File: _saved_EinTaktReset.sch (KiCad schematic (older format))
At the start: 58 parts, among them IC1 74LS624, J1 3PinTerminalBlocktg, J2 3PinTerminalBlocktg, J3 2PinTerminalBlocktg, J4 3PinTerminalBlocktg, J5 2PinTerminalBlocktg, P1 CONN_02X10, P4 CONN_02X10, SW1 SPST, SW10 SPST, SW11 SPST, SW12 SPST, SW13 SPST, SW2 SWITCH_INV, SW3 SPST, SW4 SPST, SW5 SPST, SW6 SWITCH_INV, SW7 SPST, SW8 SPST, SW9 SPST, U1 74LS132, U2 74540En, U3 74HCT541_PWR, U4 74LS32, U5 74LS00

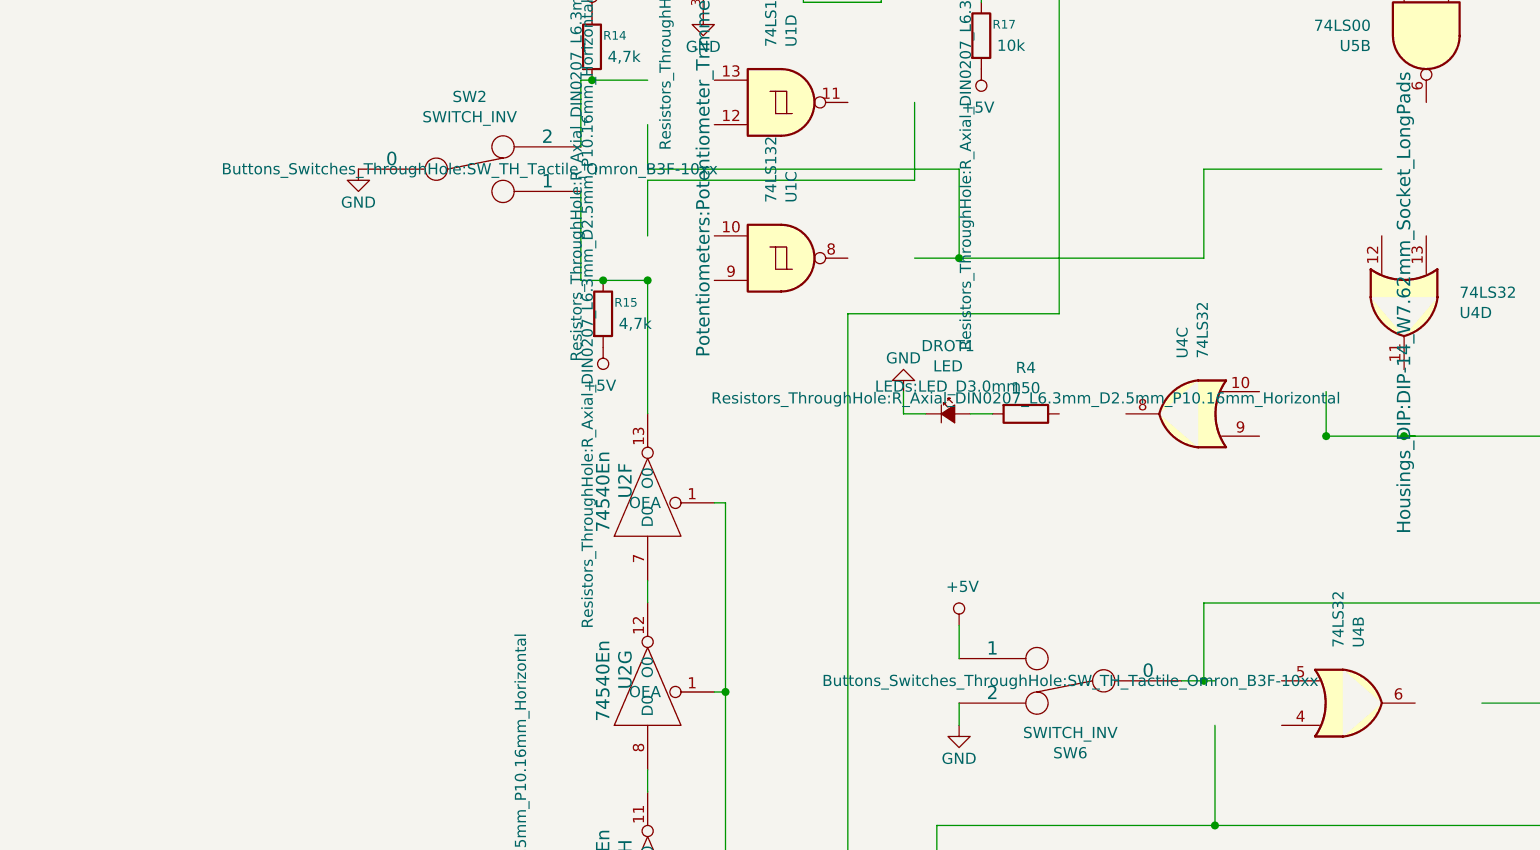
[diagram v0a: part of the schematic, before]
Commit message: Library für switches geadded
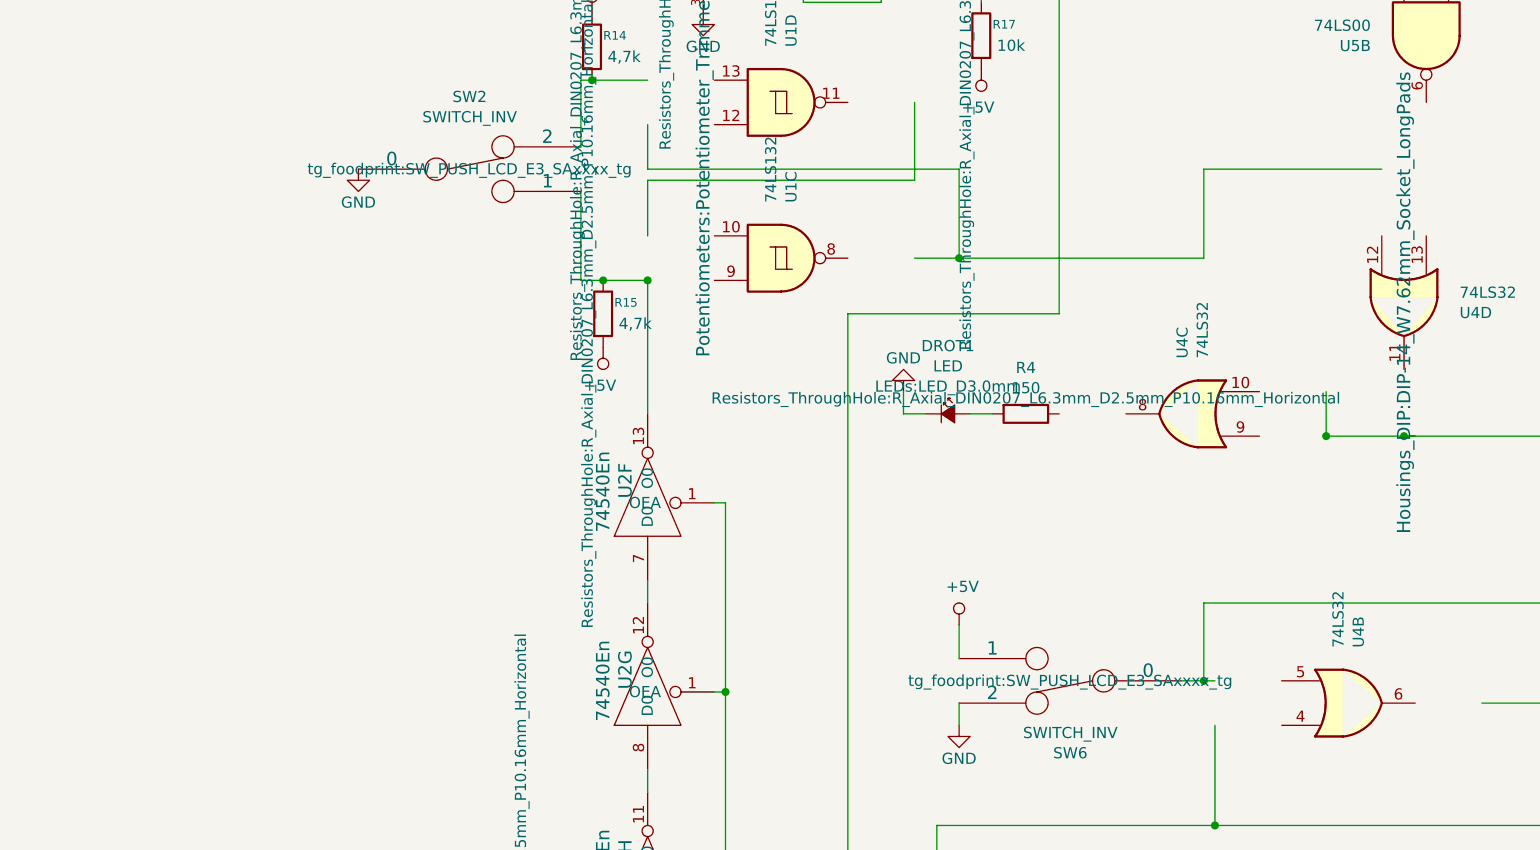
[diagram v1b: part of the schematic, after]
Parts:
- SW2, SW6: footprint Buttons_Switches_ThroughHole:SW_TH_Tactile_Omron_B3F-10xx -> tg_foodprint:SW_PUSH_LCD_E3_SAxxxx_tg
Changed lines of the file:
@@
 F 0 "SW2" H 1550 7625 50  0000 C CNN
 F 1 "SWITCH_INV" H 1550 7534 50  0000 C CNN
-F 2 "Buttons_Switches_ThroughHole:SW_TH_Tactile_Omron_B3F-10xx" H 1550 7300 50  0000 C CNN
+F 2 "tg_foodprint:SW_PUSH_LCD_E3_SAxxxx_tg" H 1550 7300 50  0000 C CNN
 F 3 "" H 1550 7300 50  0000 C CNN
 	1    1550 7300
@@
 F 0 "SW6" H 4250 9925 50  0000 C CNN
 F 1 "SWITCH_INV" H 4250 9834 50  0000 C CNN
-F 2 "Buttons_Switches_ThroughHole:SW_TH_Tactile_Omron_B3F-10xx" H 4250 9600 50  0000 C CNN
+F 2 "tg_foodprint:SW_PUSH_LCD_E3_SAxxxx_tg" H 4250 9600 50  0000 C CNN
 F 3 "" H 4250 9600 50  0000 C CNN
 	1    4250 9600
@@
 Wire Wire Line
 	2350 5950 2500 5950
+Connection ~ 2500 5950
+Wire Wire Line
+	2500 5950 3000 5950
 Wire Bus Line
 	3100 1350 3100 1500
@@
 Wire Bus Line
 	3100 1500 6550 1500
-Connection ~ 2500 5950
-Wire Wire Line
-	2500 5950 3000 5950
 $EndSCHEMATC
